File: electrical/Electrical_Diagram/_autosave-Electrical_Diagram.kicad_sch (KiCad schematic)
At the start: 28 parts

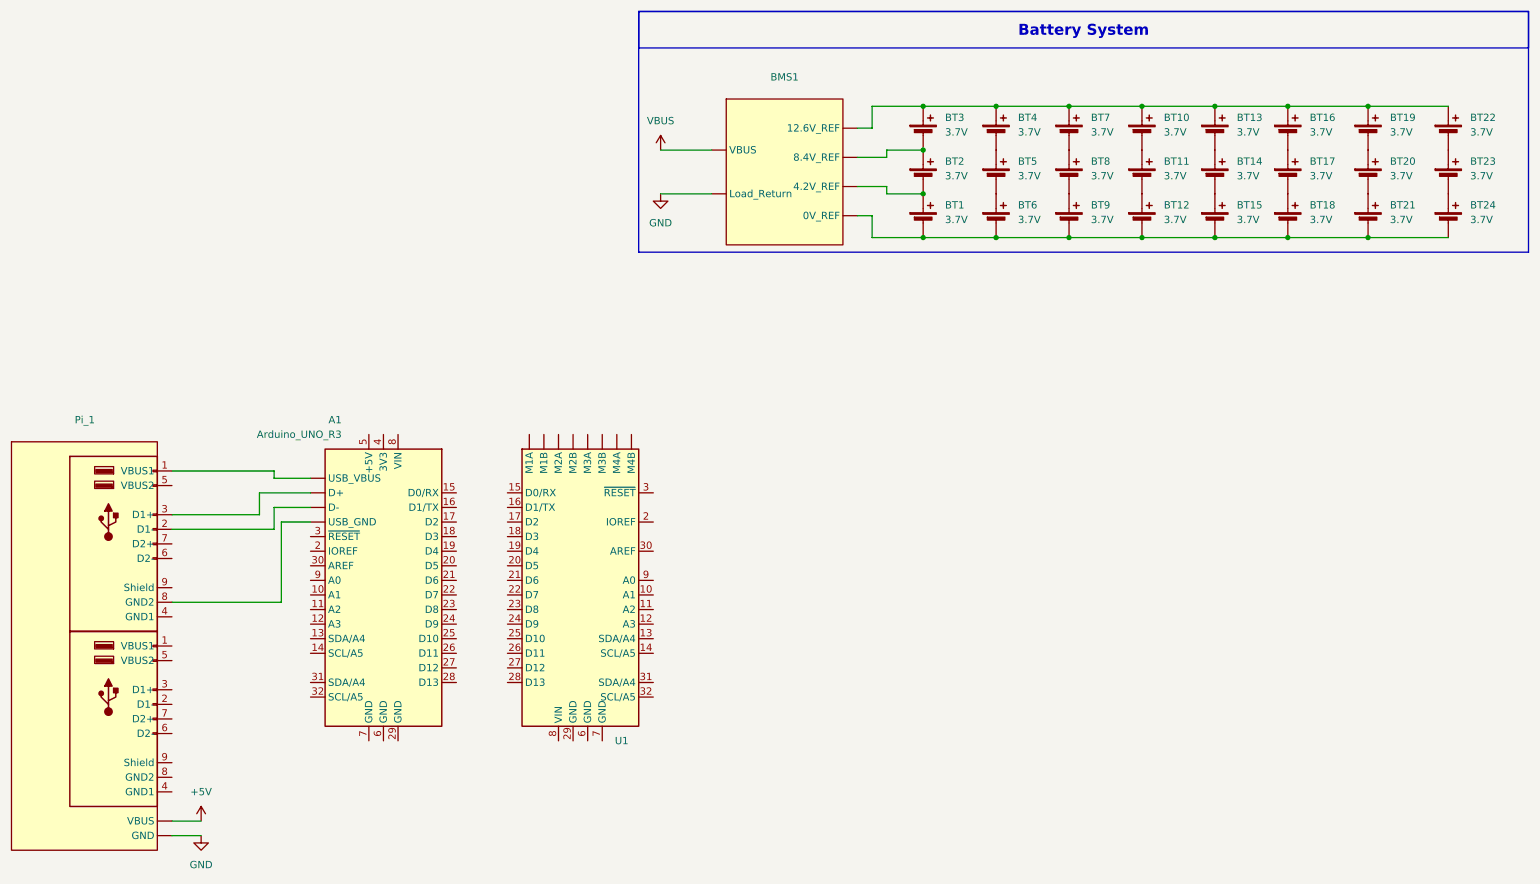
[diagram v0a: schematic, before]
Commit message: added changes to the electrical model
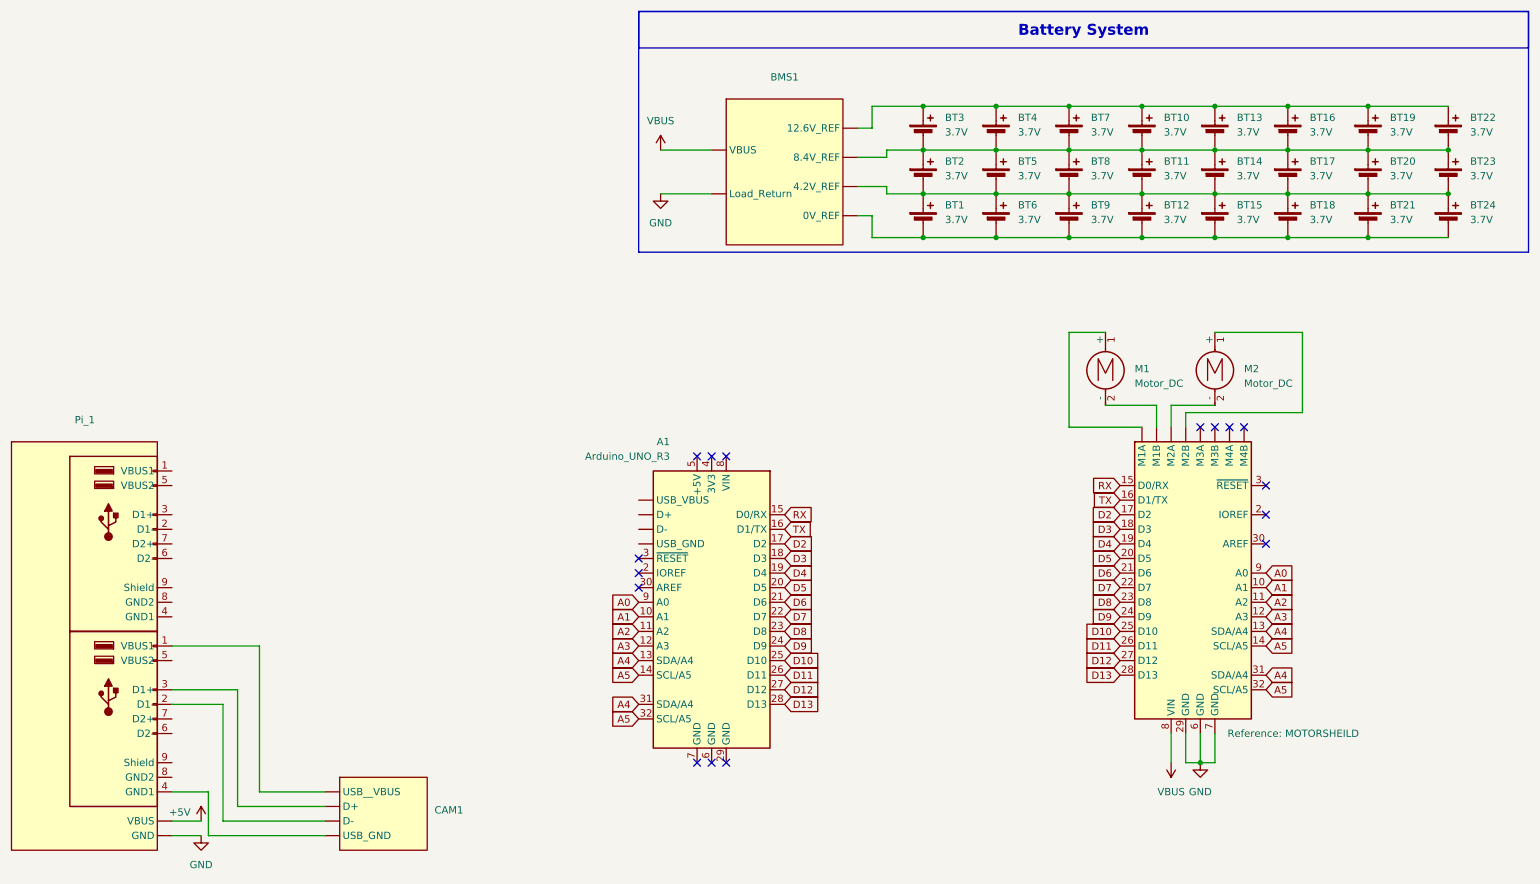
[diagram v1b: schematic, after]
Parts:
- added CAM1: ~, symbol [TT]Library:CAMERA
- added M1, M2: Motor_DC, symbol Motor:Motor_DC
- renumbered U1 to MOTORSHEILD
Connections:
- net GND: now also MOTORSHEILD.29 (GND), MOTORSHEILD.6 (GND), MOTORSHEILD.7 (GND)
- net VBUS: now also MOTORSHEILD.8 (VIN)
- net at BT23.2 (-), BT24.1 (+): now also BMS1. (VBUS), BT1.1 (+), BT11.2 (-), BT12.1 (+), BT14.2 (-), BT15.1 (+), BT17.2 (-), BT18.1 (+), BT2.2 (-), BT20.2 (-), BT21.1 (+), BT5.2 (-), BT6.1 (+), BT8.2 (-), BT9.1 (+)
- net at BT22.2 (-), BT23.1 (+): now also BMS1. (VBUS), BT10.2 (-), BT11.1 (+), BT13.2 (-), BT14.1 (+), BT16.2 (-), BT17.1 (+), BT19.2 (-), BT2.1 (+), BT20.1 (+), BT3.2 (-), BT4.2 (-), BT5.1 (+), BT7.2 (-), BT8.1 (+)
- net A1: now reaches MOTORSHEILD.10 (A1)
- net A1: now also A1.10 (A1)
- net A2: now reaches MOTORSHEILD.11 (A2)
- net A2: now also A1.11 (A2)
- net A3: now reaches MOTORSHEILD.12 (A3)
- net A3: now also A1.12 (A3)
- net A4: now reaches MOTORSHEILD.13 (SDA/A4)
- net A4: now also A1.13 (SDA/A4), A1.31 (SDA/A4), MOTORSHEILD.31 (SDA/A4)
- net A5: now reaches MOTORSHEILD.14 (SCL/A5)
- net A5: now also A1.14 (SCL/A5), A1.32 (SCL/A5), MOTORSHEILD.32 (SCL/A5)
- net RX: now reaches MOTORSHEILD.15 (D0/RX)
- net RX: now also A1.15 (D0/RX)
- net TX: now reaches MOTORSHEILD.16 (D1/TX)
- net TX: now also A1.16 (D1/TX)
- net D2: now reaches MOTORSHEILD.17 (D2)
- net D2: now also A1.17 (D2)
- net D3: now reaches MOTORSHEILD.18 (D3)
- net D3: now also A1.18 (D3)
- net D4: now reaches MOTORSHEILD.19 (D4)
- net D4: now also A1.19 (D4)
- net D5: now reaches MOTORSHEILD.20 (D5)
- net D5: now also A1.20 (D5)
- net D6: now reaches MOTORSHEILD.21 (D6)
- net D6: now also A1.21 (D6)
- net D7: now reaches MOTORSHEILD.22 (D7)
- net D7: now also A1.22 (D7)
- net D8: now reaches MOTORSHEILD.23 (D8)
- net D8: now also A1.23 (D8)
- net D9: now reaches MOTORSHEILD.24 (D9)
- net D9: now also A1.24 (D9)
- net D10: now reaches MOTORSHEILD.25 (D10)
- net D10: now also A1.25 (D10)
- net D11: now reaches MOTORSHEILD.26 (D11)
- net D11: now also A1.26 (D11)
- net D12: now reaches MOTORSHEILD.27 (D12)
- net D12: now also A1.27 (D12)
- net D13: now reaches MOTORSHEILD.28 (D13)
- net D13: now also A1.28 (D13)
- net A0: now reaches MOTORSHEILD.9 (A0)
- net A0: now also A1.9 (A0)
- net at A1. (USB_VBUS): no longer Pi_1.1 (VBUS1)
- new net: CAM1. (USB__VBUS), Pi_1.1 (VBUS1)
- new net: CAM1. (USB__VBUS), Pi_1.2 (D1-)
- new net: CAM1. (USB__VBUS), Pi_1.3 (D1+)
- new net: CAM1. (USB__VBUS), Pi_1.4 (GND1)
- new net: M2.1 (+), MOTORSHEILD. (M4B)
- new net: M2.2 (-), MOTORSHEILD. (M4B)
- new net: M1.1 (+), MOTORSHEILD. (M4B)
- new net: M1.2 (-), MOTORSHEILD. (M4B)
- now unconnected: A1. (USB_VBUS), A1. (USB_VBUS), A1. (USB_VBUS), Pi_1.2 (D1-), Pi_1.3 (D1+), Pi_1.8 (GND2)
- no-connect marks 0 -> 16
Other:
- moved on the sheet: A1, Reference: MOTORSHEILD
